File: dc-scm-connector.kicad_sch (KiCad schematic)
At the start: 55 parts, among them J1 PCB-Edge_DC-SCM-2.1_2x84_Rev-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

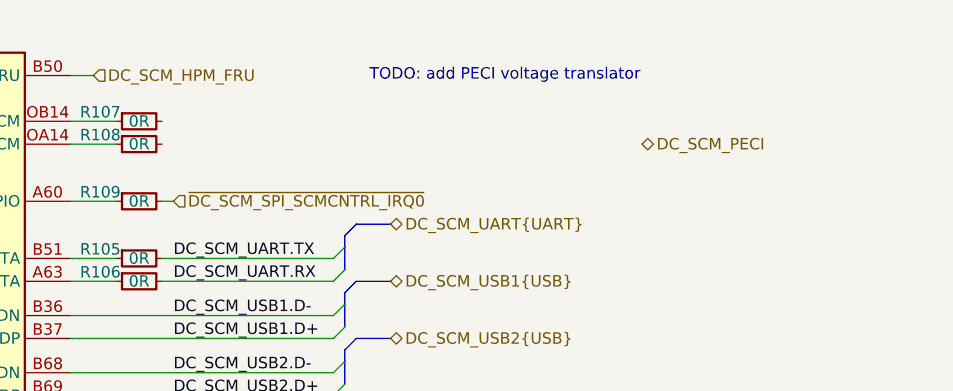
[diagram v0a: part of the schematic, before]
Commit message: [#83331] Added PECI circuitry. Small top fixes
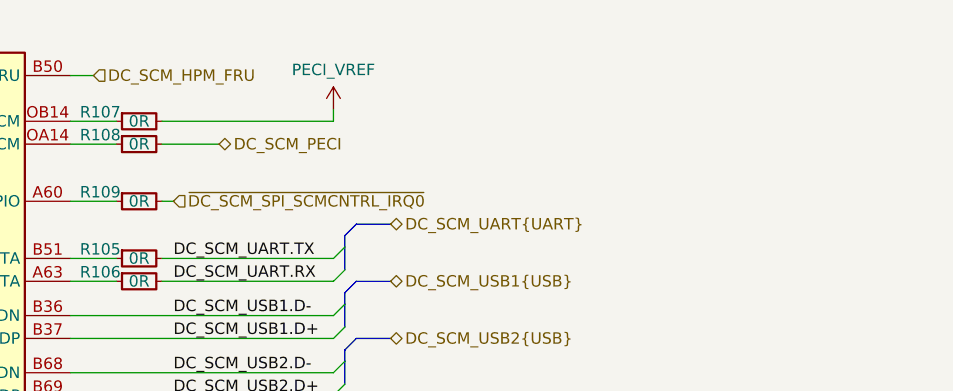
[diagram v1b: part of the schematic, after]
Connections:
- net DC_SCM_PECI: now also R108.2
- net PECI_VREF: now reaches R107.2
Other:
- note removed: "TODO: add PECI voltage translator"
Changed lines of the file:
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@@
 		)
 	)
-	(text "TODO: add PECI voltage translator"
-		(exclude_from_sim no)
-		(at 184.15 44.45 0)
-		(effects
-			(font
-				(size 1.27 1.27)
-			)
-		)
-	)
 	(no_connect
 		(at 311.15 179.07)
@@
 		)
 	)
+	(wire
+		(pts
+			(xy 165.1 49.53) (xy 146.05 49.53)
+		)
+		(stroke
+			(width 0)
+			(type default)
+		)
+	)
 	(bus
 		(pts
@@
 		)
 	)
+	(wire
+		(pts
+			(xy 165.1 48.26) (xy 165.1 49.53)
+		)
+		(stroke
+			(width 0)
+			(type default)
+		)
+	)
 	(bus
 		(pts
@@
 		)
 	)
+	(wire
+		(pts
+			(xy 152.4 52.07) (xy 146.05 52.07)
+		)
+		(stroke
+			(width 0)
+			(type default)
+		)
+	)
 	(bus
 		(pts
@@
 	(hierarchical_label "DC_SCM_PECI"
 		(shape bidirectional)
-		(at 199.39 52.07 0)
+		(at 152.4 52.07 0)
 		(effects
 			(font
@@
 					(unit 1)
 				)
+			)
+		)
+	)
+	(symbol
+		(lib_id "antmicropower:+0V5")
+		(at 165.1 48.26 0)
+		(unit 1)
+		(exclude_from_sim no)
+		(in_bom yes)
+		(on_board yes)
+		(dnp no)
+		(property "Reference" "#PWR0242"
+			(at 165.1 52.07 0)
+			(effects
+				(font
+					(size 1.27 1.27)
+				)
+				(hide yes)
+			)
+		)
+		(property "Value" "PECI_VREF"
+			(at 165.1 43.815 0)
+			(effects
+				(font
+					(size 1.27 1.27)
+				)
+			)
+		)
+		(property "Footprint" ""
+			(at 165.1 48.26 0)
+			(effects
+				(font
+					(size 1.27 1.27)
+				)
+				(hide yes)
+			)
+		)
+		(property "Datasheet" ""
+			(at 165.1 48.26 0)
+			(effects
+				(font
+					(size 1.27 1.27)
+				)
+				(hide yes)
+			)
+		)
+		(property "Description" ""
+			(at 165.1 48.26 0)
+			(effects
+				(font
+					(size 1.27 1.27)
+				)
+				(hide yes)
+			)
+		)
+		(pin "1"
+		)
+		(instances
+			(project ""
+				(path "/5f636c45-3c15-4731-8931-4625e0dab7e4/ca214ec5-42cf-4efd-9251-fb98a8d45893"
+					(reference "#PWR0242")
+					(unit 1)
+				)

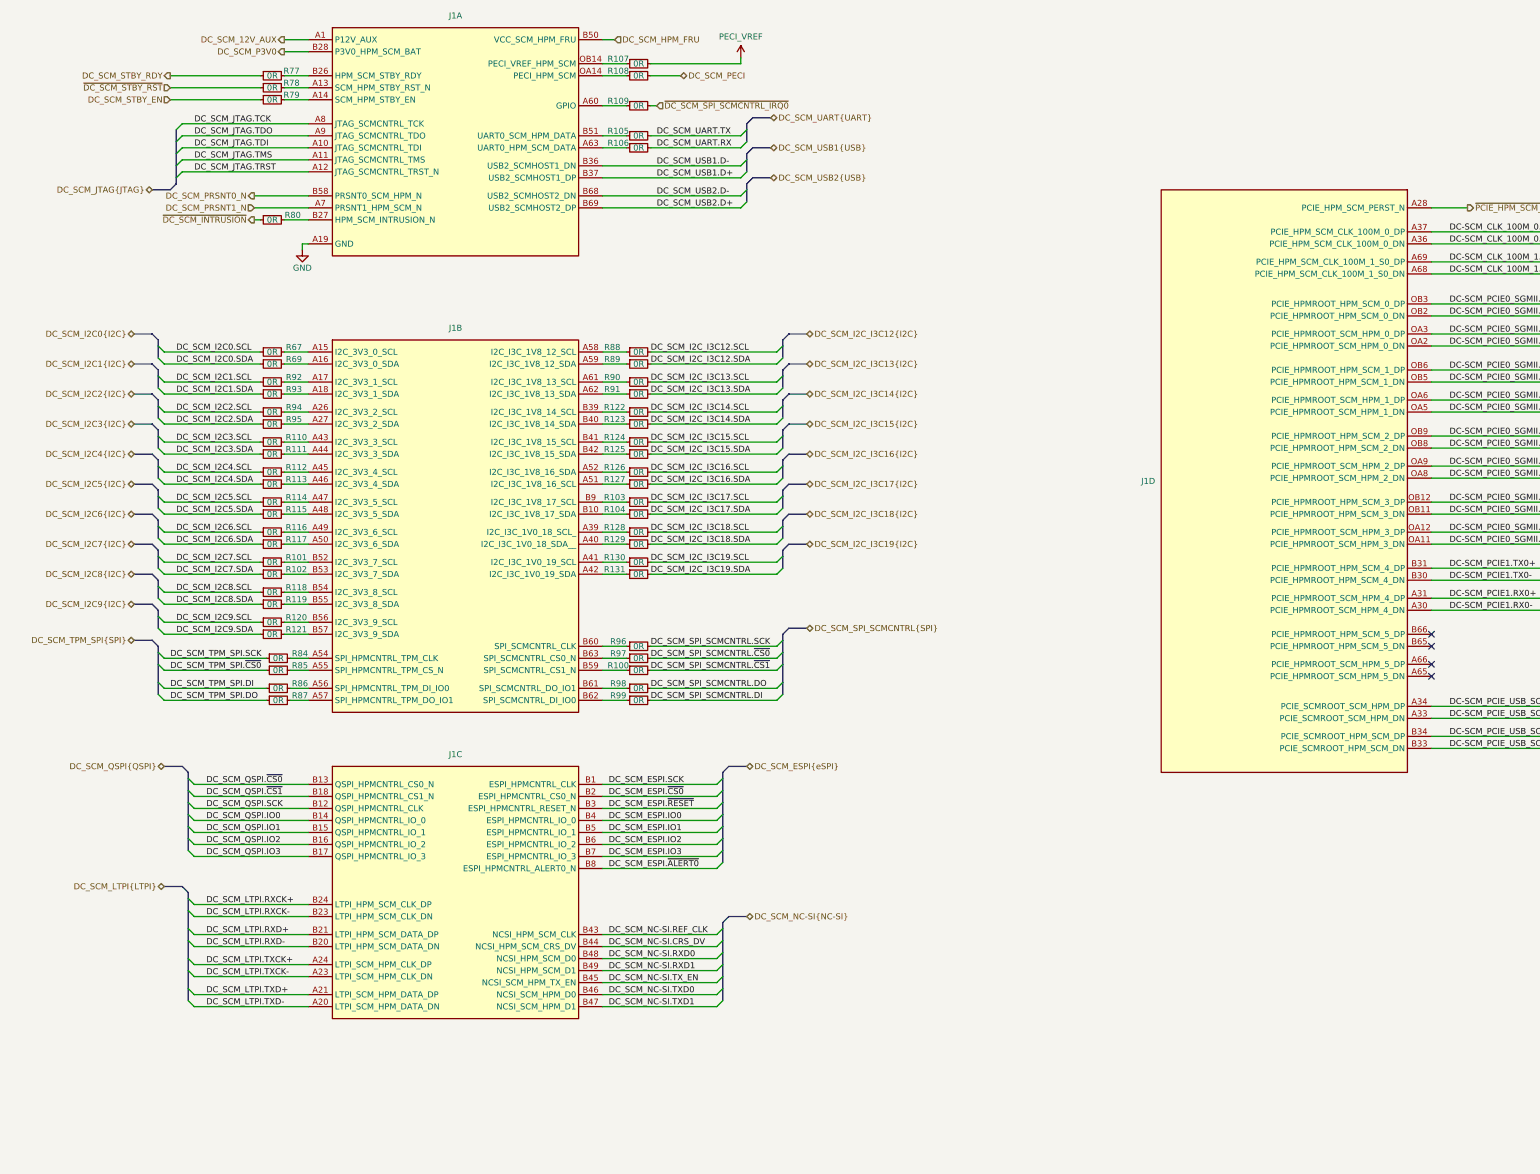
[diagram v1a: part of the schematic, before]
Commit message: [#83362] Add headers to LTPI, PECI and I2C
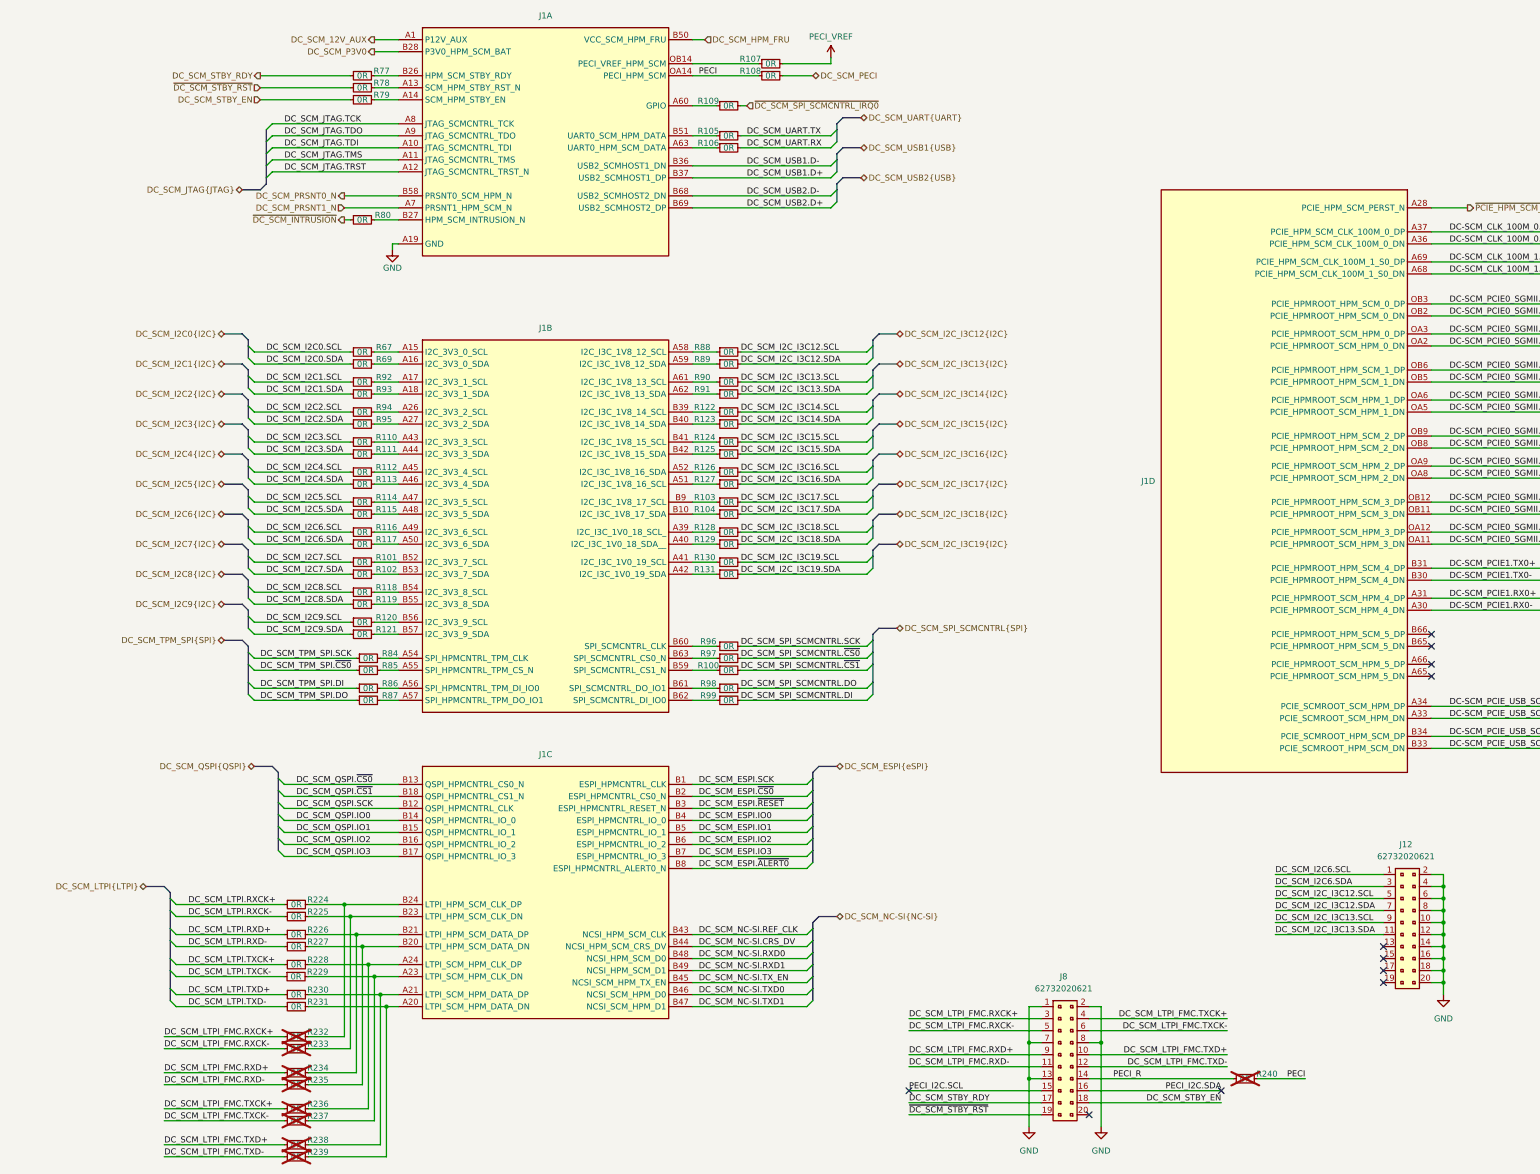
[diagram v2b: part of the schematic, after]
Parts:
- added J12, J8: PinHeader_2x10_P1.27mm_SMD_Shrouded, antmicro-footprints:PinHeader_2x10_P1.27mm_SMD_Shrouded, symbol antmicroGenericPinHeaders:PinHeader_2x10_P1.27mm_SMD_Shrouded
- added R224, R225, R226, R227, R228, R229, R230, R231, R232, R233, R234, R235, R236, R237, R238, R239, R240: R_0R_0402, antmicro-footprints:R_0402_1005Metric, symbol antmicroResistors0402:R_0R_0402
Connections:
- net DC_SCM_I2C6.SCL: now also J12.1
- net DC_SCM_I2C6.SDA: now also J12.3
- net DC_SCM_I2C_I3C12.SCL: now also J12.5
- net DC_SCM_I2C_I3C12.SDA: now also J12.7
- net DC_SCM_I2C_I3C13.SCL: now also J12.9
- net DC_SCM_I2C_I3C13.SDA: now also J12.11
- net DC_SCM_LTPI.RXCK+: now also R224.1; no longer J1.B24 (LTPI_HPM_SCM_CLK_DP)
- net DC_SCM_LTPI.RXCK-: now also R225.1; no longer J1.B23 (LTPI_HPM_SCM_CLK_DN)
- net DC_SCM_LTPI.RXD+: now also R226.1; no longer J1.B21 (LTPI_HPM_SCM_DATA_DP)
- net DC_SCM_LTPI.RXD-: now also R227.1; no longer J1.B20 (LTPI_HPM_SCM_DATA_DN)
- net DC_SCM_LTPI.TXCK+: now also R228.1; no longer J1.A24 (LTPI_SCM_HPM_CLK_DP)
- net DC_SCM_LTPI.TXCK-: now also R229.1; no longer J1.A23 (LTPI_SCM_HPM_CLK_DN)
- net DC_SCM_LTPI.TXD+: now also R230.1; no longer J1.A21 (LTPI_SCM_HPM_DATA_DP)
- net DC_SCM_LTPI.TXD-: now also R231.1; no longer J1.A20 (LTPI_SCM_HPM_DATA_DN)
- net DC_SCM_STBY_EN: now also J8.18
- net DC_SCM_STBY_RDY: now also J8.17
- net GND: now also J12.10, J12.12, J12.14, J12.16, J12.18, J12.2, J12.20, J12.4, J12.6, J12.8, J8.1, J8.13, J8.2, J8.7, J8.8
- net ~{DC_SCM_STBY_RST}: now also J8.19
- net PECI: now reaches J1.OA14 (PECI_HPM_SCM), R108.1
- net PECI: now also R240.2
- new net: J1.A21 (LTPI_SCM_HPM_DATA_DP), R230.2, R238.2
- new net: J1.B23 (LTPI_HPM_SCM_CLK_DN), R225.2, R233.2
- new net: J1.B24 (LTPI_HPM_SCM_CLK_DP), R224.2, R232.2
- new net: J1.A24 (LTPI_SCM_HPM_CLK_DP), R228.2, R236.2
- new net: J1.B21 (LTPI_HPM_SCM_DATA_DP), R226.2, R234.2
- new net: J1.B20 (LTPI_HPM_SCM_DATA_DN), R227.2, R235.2
- new net: J1.A20 (LTPI_SCM_HPM_DATA_DN), R231.2, R239.2
- new net: J1.A23 (LTPI_SCM_HPM_CLK_DN), R229.2, R237.2
- new net DC_SCM_LTPI_FMC.RXCK+: J8.3, R232.1
- new net DC_SCM_LTPI_FMC.RXCK-: J8.5, R233.1
- new net DC_SCM_LTPI_FMC.RXD+: J8.9, R234.1
- new net DC_SCM_LTPI_FMC.RXD-: J8.11, R235.1
- new net DC_SCM_LTPI_FMC.TXCK+: J8.4, R236.1
- new net DC_SCM_LTPI_FMC.TXCK-: J8.6, R237.1
- new net DC_SCM_LTPI_FMC.TXD+: J8.10, R238.1
- new net DC_SCM_LTPI_FMC.TXD-: J8.12, R239.1
- new net PECI_I2C.SCL: J8.15
- new net PECI_I2C.SDA: J8.16
- new net PECI_R: J8.14, R240.1
- no-connect marks 4 -> 11
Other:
- moved on the sheet: J1A, J1B, J1C, R100, R101, R102, R103, R104, R105, R106, R107, R108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

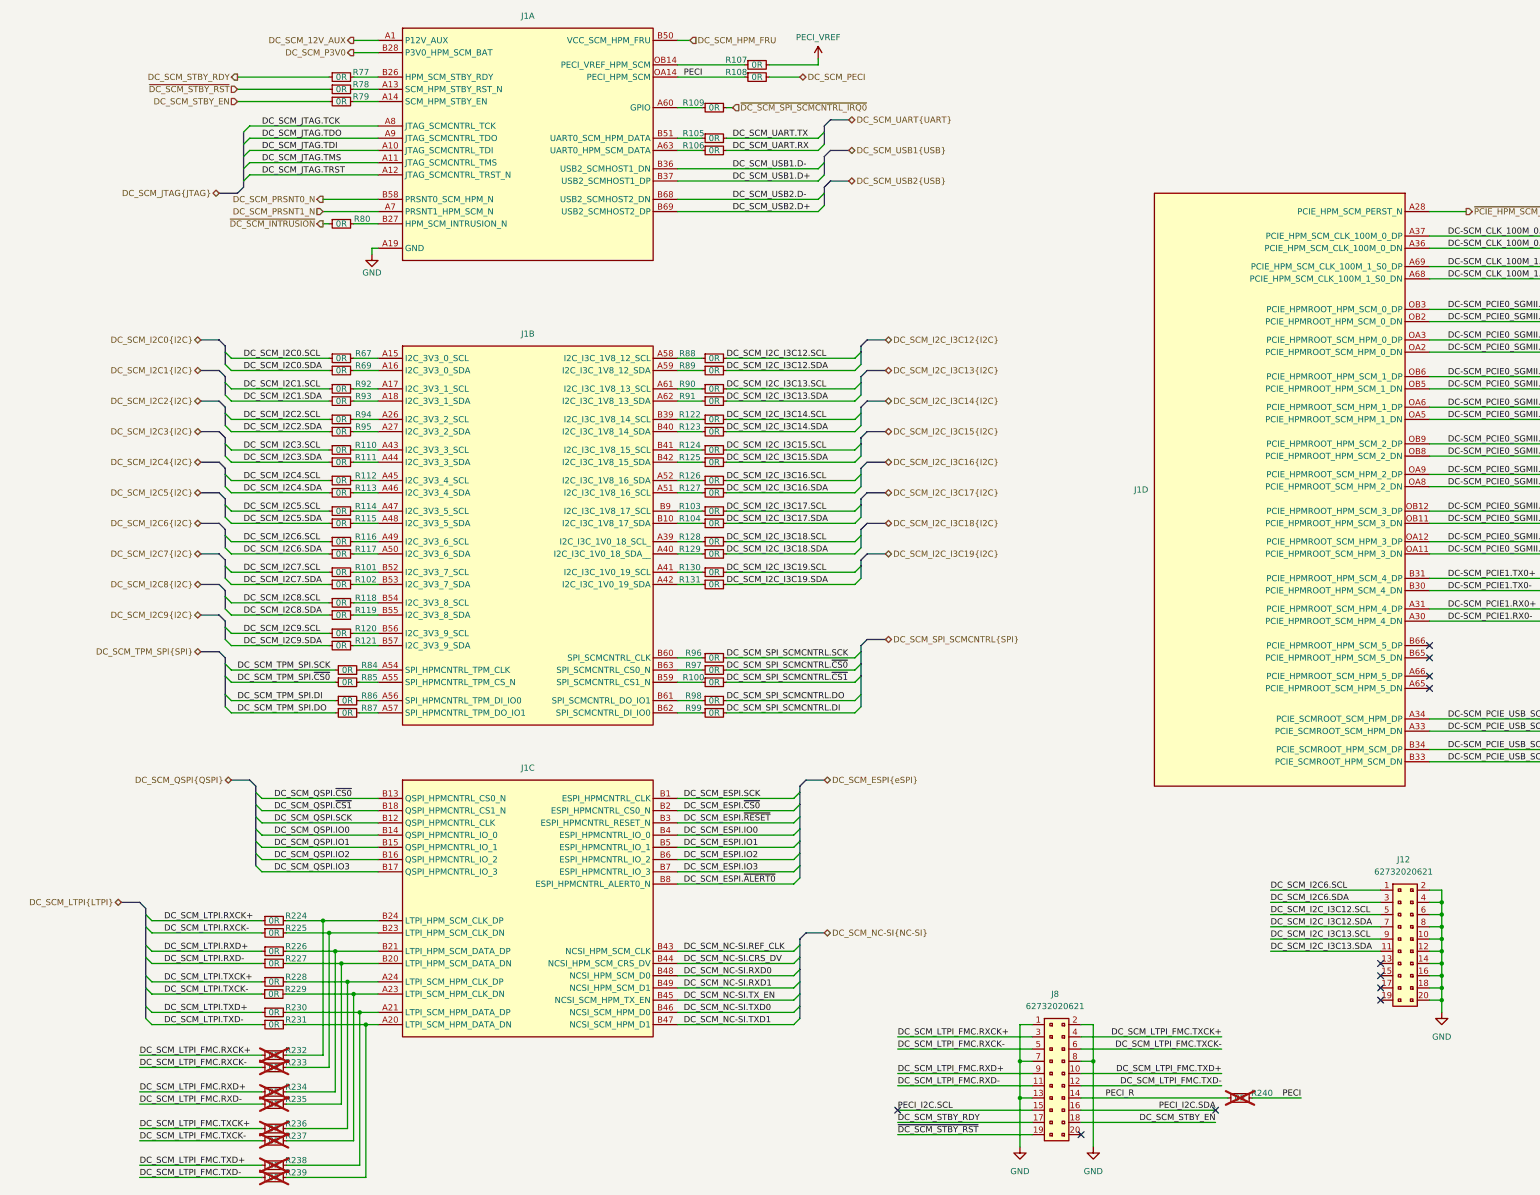
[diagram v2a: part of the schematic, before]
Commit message: [#83362] Fix connections of headers, add I2C mux
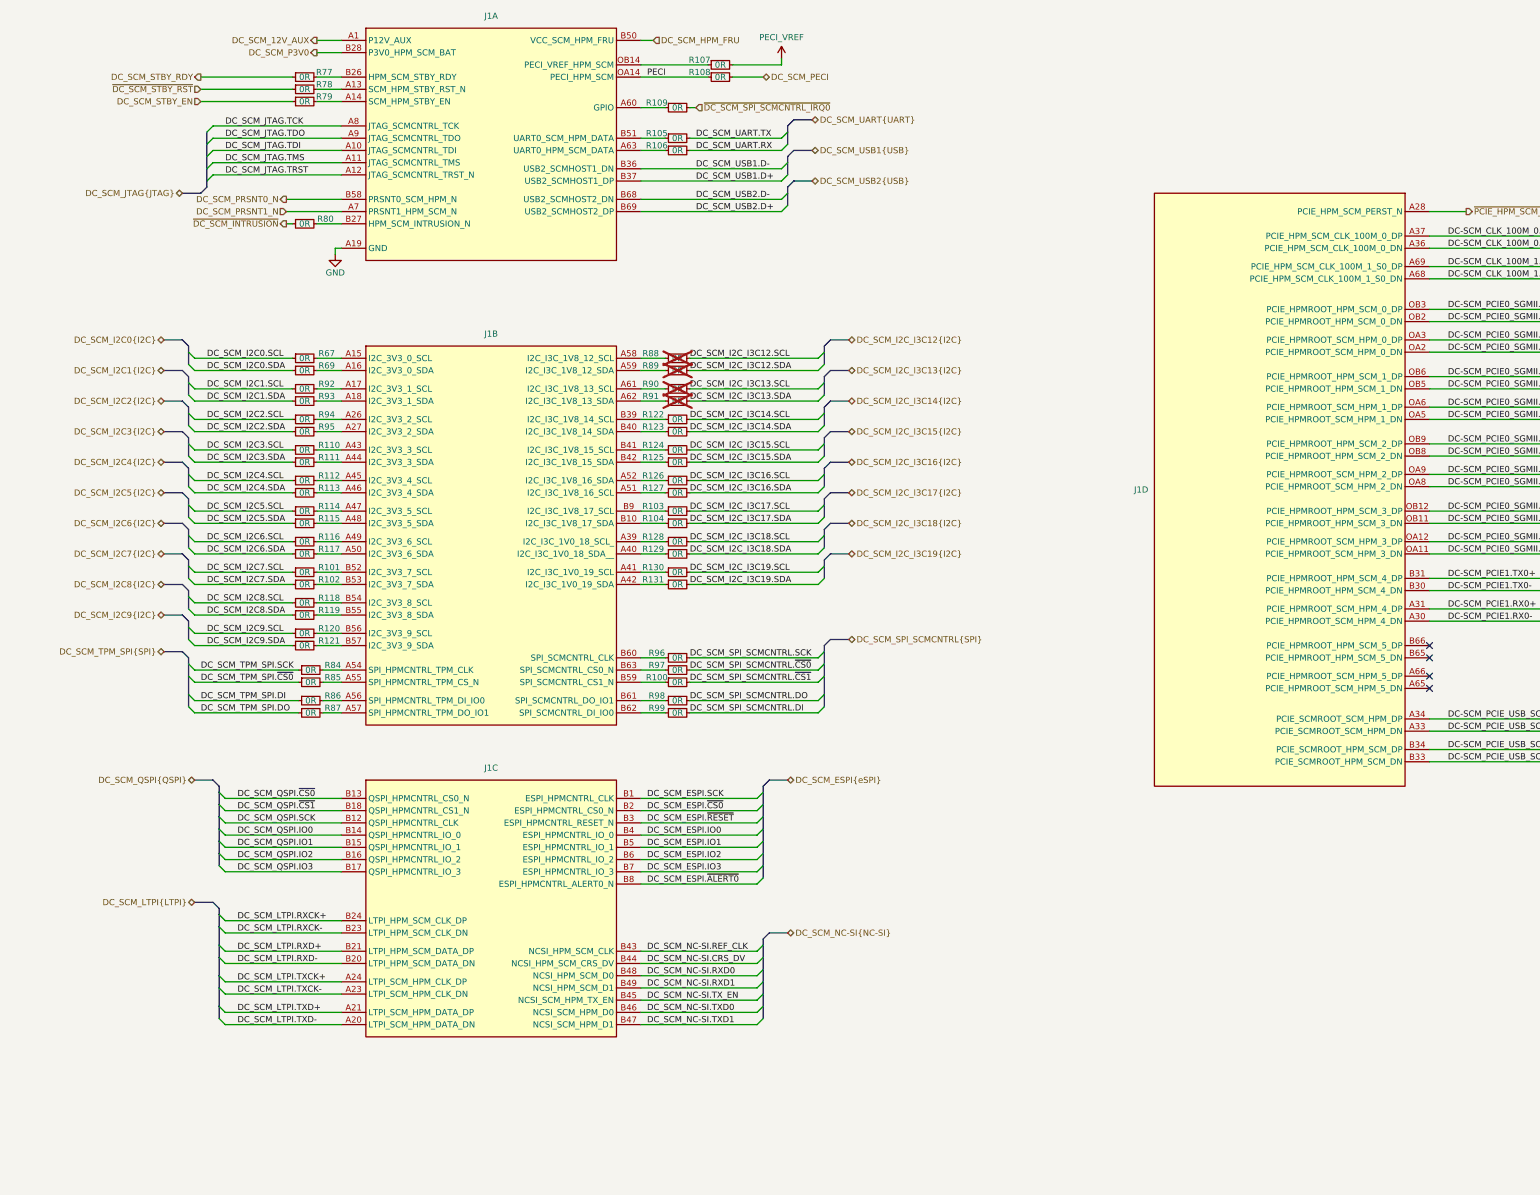
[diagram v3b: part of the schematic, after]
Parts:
- removed J12, J8: PinHeader_2x10_P1.27mm_SMD_Shrouded, antmicro-footprints:PinHeader_2x10_P1.27mm_SMD_Shrouded, symbol antmicroGenericPinHeaders:PinHeader_2x10_P1.27mm_SMD_Shrouded
- removed R224, R225, R226, R227, R228, R229, R230, R231, R232, R233, R234, R235, R236, R237, R238, R239, R240: R_0R_0402, antmicro-footprints:R_0402_1005Metric, symbol antmicroResistors0402:R_0R_0402
- R88, R89, R90, R91: now not fitted
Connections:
- net DC_SCM_LTPI.RXCK+: now also J1.B24 (LTPI_HPM_SCM_CLK_DP)
- net DC_SCM_LTPI.RXCK-: now also J1.B23 (LTPI_HPM_SCM_CLK_DN)
- net DC_SCM_LTPI.RXD+: now also J1.B21 (LTPI_HPM_SCM_DATA_DP)
- net DC_SCM_LTPI.RXD-: now also J1.B20 (LTPI_HPM_SCM_DATA_DN)
- net DC_SCM_LTPI.TXCK+: now also J1.A24 (LTPI_SCM_HPM_CLK_DP)
- net DC_SCM_LTPI.TXCK-: now also J1.A23 (LTPI_SCM_HPM_CLK_DN)
- net DC_SCM_LTPI.TXD+: now also J1.A21 (LTPI_SCM_HPM_DATA_DP)
- net DC_SCM_LTPI.TXD-: now also J1.A20 (LTPI_SCM_HPM_DATA_DN)
- no-connect marks 11 -> 4
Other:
- moved on the sheet: J1A, J1B, J1C, R100, R101, R102, R103, R104, R105, R106, R107, R108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

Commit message: [#83609] Reannotate board
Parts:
- renumbered R77 to R1, R95 to R10, R110 to R11, R111 to R12, R112 to R13, R113 to R14, R114 to R15, R115 to R16, R116 to R17, R117 to R18, R101 to R19, R78 to R2, R102 to R20, R118 to R21, R119 to R22, R120 to R23, R121 to R24, R84 to R25, R85 to R26, R86 to R27, R87 to R28, R109 to R29, R79 to R3, R105 to R30, R106 to R31, R88 to R32, R89 to R33, R90 to R34, R91 to R35, R122 to R36, R123 to R37, R124 to R38, R125 to R39, R80 to R4, R126 to R40, R127 to R41, R103 to R42, R104 to R43, R128 to R44, R129 to R45, R130 to R46, R131 to R47, R96 to R48, R97 to R49, R67 to R5, R100 to R50, R98 to R51, R99 to R52, R107 to R53, R108 to R54, R69 to R6, R92 to R7, R93 to R8, R94 to R9
